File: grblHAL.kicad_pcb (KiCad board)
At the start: 4 copper layers, 150 x 105 mm, 279 parts, among them J1 Screw_Terminal_01x08, J10 Screw_Terminal_01x08, J11 Screw_Terminal_01x04x3, J12 Screw_Terminal_01x02, J13 Conn_ARM_JTAG_SWD_10, J14 Conn_01x03_Pin, J15 Conn_01x03_Pin, J16 Conn_01x02_Pin, J17 Conn_01x02_Pin, J18 Conn_01x03_Pin, J19 Screw_Terminal_01x02x5, J2 Screw_Terminal_01x08, J20 Conn_01x02_Pin, J21 Screw_Terminal_01x02, J22 Screw_Terminal_01x04x3, J23 Conn_01x03_Pin, J24 Conn_01x03_Pin, J25 Conn_01x03_Pin, J26 Conn_01x03_Pin, J27 Conn_01x03_Pin, J28 Conn_01x03_Pin, J29 Conn_01x03_Pin, J3 Screw_Terminal_01x08, J30 Conn_01x03_Pin, J31 Conn_01x03_Pin, J32 Conn_01x03_Pin, J33 Conn_01x03_Pin, J34 Conn_01x03_Pin, J35 Conn_01x03_Pin, J36 Conn_01x03_Pin, J37 Conn_01x03_Pin, J38 Conn_01x03_Pin, J39 Conn_01x03_Pin, J4 Screw_Terminal_01x06, J40 Conn_01x03_Pin, J41 Conn_01x03_Pin, J42 Conn_01x03_Pin, J43 USB_B, J44 Conn_01x08_Pin, J5 Screw_Terminal_01x06, J6 Screw_Terminal_01x02, J7 Screw_Terminal_01x08, J8 Screw_Terminal_01x02, J9 Screw_Terminal_01x08, SW1 SW_Push, SW2 SW_Push, U1 STM32F407VETx, U10 74HC2G34, U11 74HC2G34, U12 74HC2G34, U13 74HC2G34, U14 74HC2G34, U15 MCP6004, U16 ULN2803A, U17 ELQ3H4(TA)-G, U18 ELQ3H4(TA)-G, U19 ELQ3H4(TA)-G, U2 MAX3078E, U20 ELQ3H4(TA)-G, U21 74HC2G34, U22 74HC2G34, U23 74HC2G34, U24 USBLC6-2P6, U25 LM358, U26 SN74LVC245APW, U3 AMS1117-3.3, U4 LMR51430, U5 LMR51430, U6 MCP6004, U7 ELQ3H4(TA)-G, U8 74HC2G34, U9 74HC2G34, Y1 8Mhz

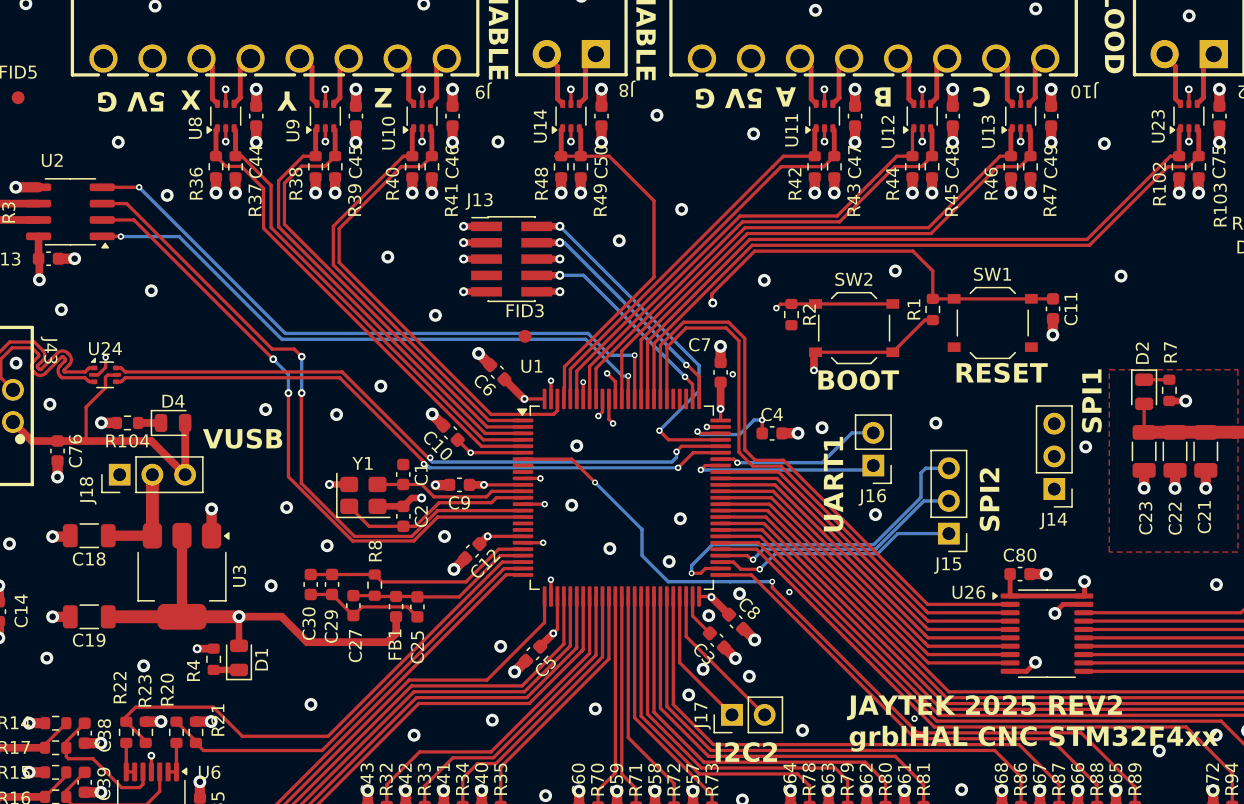
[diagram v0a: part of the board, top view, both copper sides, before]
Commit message: corrected top silk
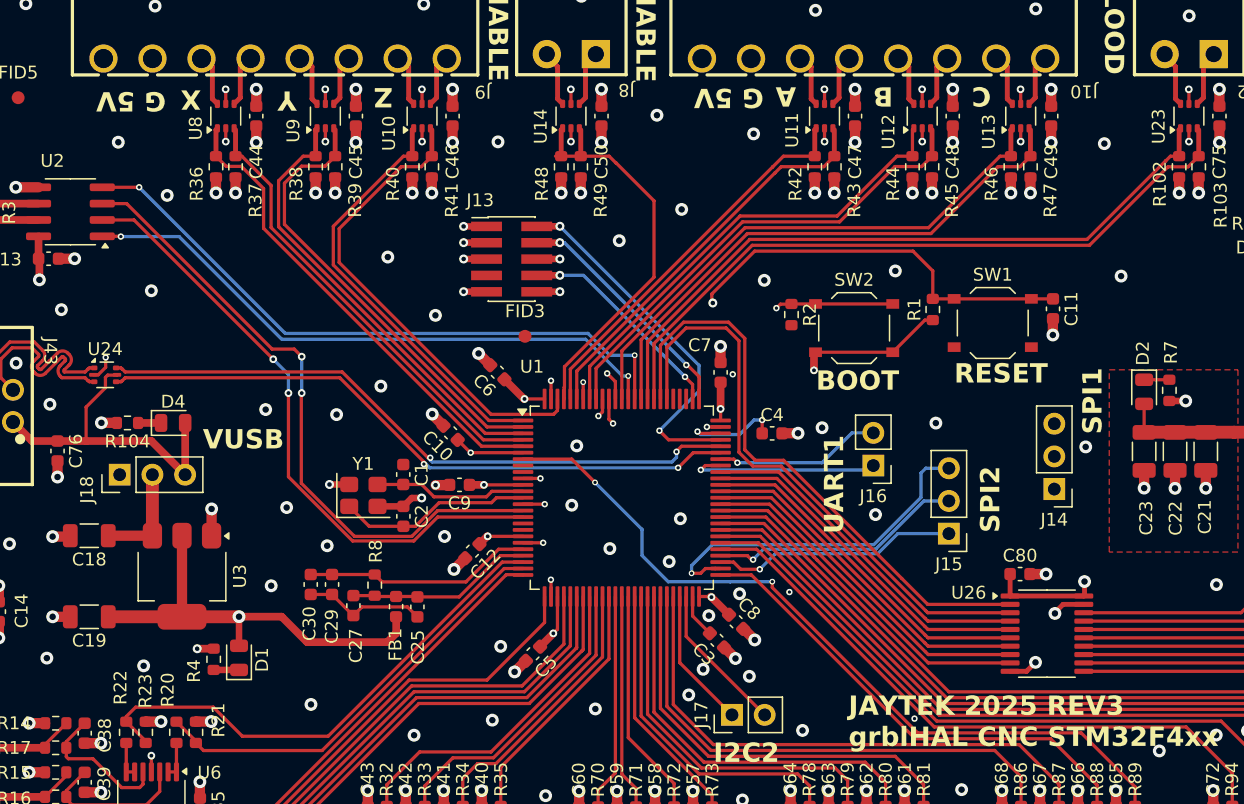
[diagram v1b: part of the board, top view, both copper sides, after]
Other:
- board text added: "G 5V"
- board text added: "JAYTEK 2025 REV3 grblHAL CNC STM32F4xx"
- board text removed: "JAYTEK 2025 REV2 grblHAL CNC STM32F4xx"
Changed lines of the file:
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@@
 		)
 	)
-	(gr_text "5V G"
+	(gr_text "G 5V"
 		(at 105.49 45.44 180)
 		(layer "F.SilkS")
@@
 		)
 	)
-	(gr_text "JAYTEK 2025 REV2\ngrblHAL CNC STM32F4xx\n\n"
+	(gr_text "JAYTEK 2025 REV3\ngrblHAL CNC STM32F4xx\n\n"
 		(at 158.51 99.01 0)
 		(layer "F.SilkS")
@@
 		)
 	)
-	(gr_text "5V G"
+	(gr_text "G 5V"
 		(at 151.93 45.18 180)
 		(layer "F.SilkS")
